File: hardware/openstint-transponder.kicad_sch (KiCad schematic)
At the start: 32 parts, among them J1 V+, J2 V-, Q1 AO3401A, U1 STM32C011F4Ux, U3 UCC27517DBV, U4 TLV760xx, Y1 20 MHz

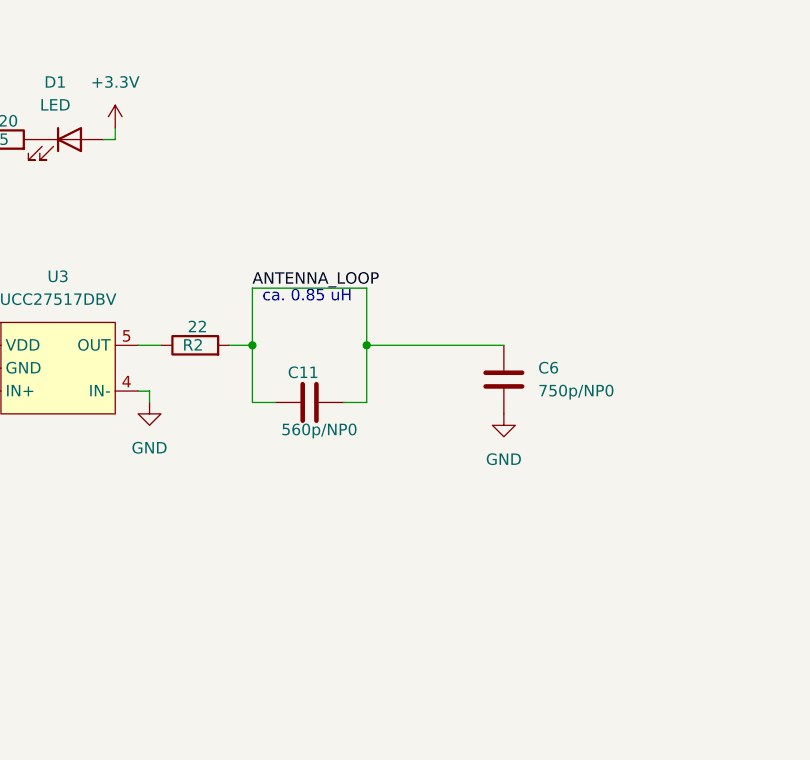
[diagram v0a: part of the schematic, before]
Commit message: antenna re-tuned
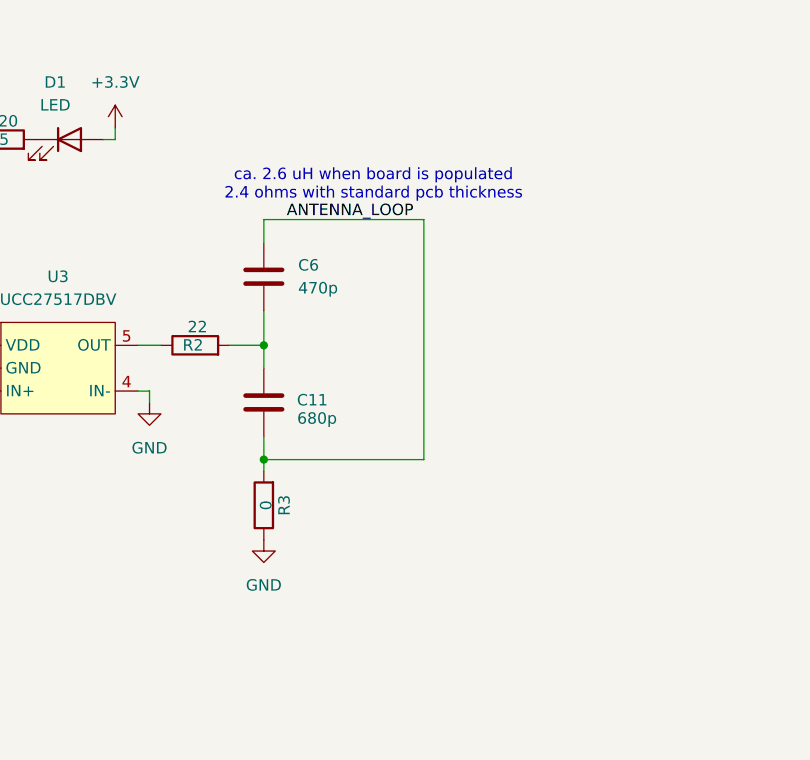
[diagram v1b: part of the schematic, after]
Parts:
- added R3: 0, Resistor_SMD:R_0402_1005Metric, symbol Device:R
- C11: value 560p/NP0 -> 680p; LCSC C107054 -> C30816
- C6: value 750p/NP0 -> 470p; LCSC C113798 -> C1620
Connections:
- net ANTENNA_LOOP: now also R3.2; no longer C11.1, R2.2
- net GND: now also R3.1; no longer C6.2
- new net: C11.1, C6.2, R2.2
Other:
- note added: "ca. 2.6 uH when board is populated 2.4 ohms with standard pcb thickness"
- note removed: "ca. 0.85 uH"
- moved on the sheet: C11, C6
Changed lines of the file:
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@@
 	(generator_version "9.0")
 	(paper "A4")
-	(text "ca. 0.85 uH"
+	(text "ca. 2.6 uH when board is populated\n2.4 ohms with standard pcb thickness"
 		(exclude_from_sim no)
-		(at 185.166 117.856 0)
+		(at 192.532 105.41 0)
 		(effects
 			(font
@@
 	)
 	(junction
-		(at 179.07 123.19)
+		(at 180.34 135.89)
 		(diameter 0)
 		(color 0 0 0 0)
@@
 	)
 	(junction
-		(at 191.77 123.19)
+		(at 180.34 123.19)
 		(diameter 0)
 		(color 0 0 0 0)
@@
 	(wire
 		(pts
+			(xy 180.34 111.76) (xy 180.34 109.22)
+		)
+		(stroke
+			(width 0)
+			(type default)
+		)
+	)
+	(wire
+		(pts
 			(xy 196.85 49.53) (xy 196.85 64.77)
 		)
@@
 	(wire
 		(pts
-			(xy 191.77 116.84) (xy 191.77 123.19)
+			(xy 198.12 109.22) (xy 198.12 135.89)
 		)
 		(stroke
@@
 	(wire
 		(pts
-			(xy 191.77 123.19) (xy 191.77 129.54)
-		)
-		(stroke
-			(width 0)
-			(type default)
-		)
-	)
-	(wire
-		(pts
 			(xy 116.84 118.11) (xy 116.84 119.38)
 		)
@@
 	(wire
 		(pts
-			(xy 127 119.38) (xy 129.54 119.38)
+			(xy 180.34 123.19) (xy 180.34 125.73)
 		)
 		(stroke
@@
 	(wire
 		(pts
-			(xy 33.02 49.53) (xy 33.02 50.8)
+			(xy 127 119.38) (xy 129.54 119.38)
 		)
 		(stroke
@@
 	(wire
 		(pts
-			(xy 207.01 123.19) (xy 191.77 123.19)
+			(xy 33.02 49.53) (xy 33.02 50.8)
 		)
 		(stroke
@@
 	(wire
 		(pts
+			(xy 180.34 133.35) (xy 180.34 135.89)
+		)
+		(stroke
+			(width 0)
+			(type default)
+		)
+	)
+	(wire
+		(pts
 			(xy 214.63 43.18) (xy 214.63 44.45)
 		)
@@
 	(wire
 		(pts
-			(xy 176.53 123.19) (xy 179.07 123.19)
+			(xy 176.53 123.19) (xy 180.34 123.19)
 		)
 		(stroke
@@
 	(wire
 		(pts
-			(xy 189.23 129.54) (xy 191.77 129.54)
+			(xy 68.58 43.18) (xy 74.93 43.18)
 		)
 		(stroke
@@
 	(wire
 		(pts
-			(xy 68.58 43.18) (xy 74.93 43.18)
+			(xy 180.34 119.38) (xy 180.34 123.19)
 		)
 		(stroke
@@
 	(wire
 		(pts
-			(xy 179.07 123.19) (xy 179.07 116.84)
-		)
-		(stroke
-			(width 0)
-			(type default)
-		)
-	)
-	(wire
-		(pts
 			(xy 167.64 129.54) (xy 167.64 128.27)
 		)
@@
 	(wire
 		(pts
-			(xy 179.07 129.54) (xy 179.07 123.19)
+			(xy 180.34 109.22) (xy 198.12 109.22)
 		)
 		(stroke
@@
 	(wire
 		(pts
+			(xy 180.34 135.89) (xy 180.34 137.16)
+		)
+		(stroke
+			(width 0)
+			(type default)
+		)
+	)
+	(wire
+		(pts
 			(xy 83.82 22.86) (xy 83.82 21.59)
 		)
@@
 	(wire
 		(pts
-			(xy 181.61 129.54) (xy 179.07 129.54)
+			(xy 274.32 59.69) (xy 274.32 58.42)
 		)
 		(stroke
@@
 	(wire
 		(pts
-			(xy 274.32 59.69) (xy 274.32 58.42)
+			(xy 158.75 44.45) (xy 171.45 44.45)
 		)
 		(stroke
@@
 	(wire
 		(pts
-			(xy 158.75 44.45) (xy 171.45 44.45)
+			(xy 54.61 49.53) (xy 55.88 49.53)
 		)
 		(stroke
@@
 	(wire
 		(pts
-			(xy 54.61 49.53) (xy 55.88 49.53)
+			(xy 180.34 135.89) (xy 198.12 135.89)
 		)
 		(stroke
@@
 		)
 	)
-	(wire
-		(pts
-			(xy 179.07 116.84) (xy 191.77 116.84)
-		)
-		(stroke
-			(width 0)
-			(type default)
-		)
-	)
 	(label "V_PUSHPULL"
 		(at 130.81 119.38 0)
@@
 	)
 	(label "ANTENNA_LOOP"
-		(at 179.07 116.84 0)
+		(at 182.88 109.22 0)
 		(effects
 			(font
@@
 	(symbol
 		(lib_id "Device:C")
-		(at 207.01 127 0)
+		(at 180.34 115.57 0)
 		(unit 1)
 		(exclude_from_sim no)
@@
 		(fields_autoplaced yes)
 		(property "Reference" "C6"
-			(at 210.82 125.7299 0)
+			(at 184.15 114.2999 0)
 			(effects
 				(font
@@
 			)
 		)
-		(property "Value" "750p/NP0"
-			(at 210.82 128.2699 0)
+		(property "Value" "470p"
+			(at 184.15 116.8399 0)
 			(effects
 				(font
@@
 		)
 		(property "Footprint" "Capacitor_SMD:C_0603_1608Metric"
-			(at 207.9752 130.81 0)
+			(at 181.3052 119.38 0)
 			(effects
 				(font
@@
 		)
 		(property "Datasheet" "~"
-			(at 207.01 127 0)
+			(at 180.34 115.57 0)
 			(effects
 				(font
@@
 		)
 		(property "Description" "Unpolarized capacitor"
-			(at 207.01 127 0)
+			(at 180.34 115.57 0)
 			(effects
 				(font
@@
 			)
 		)
-		(property "LCSC" "C113798"
-			(at 207.01 127 90)
+		(property "LCSC" "C1620"
+			(at 180.34 115.57 90)
 			(effects
 				(font
@@
 	(symbol
 		(lib_id "power:GND")
-		(at 207.01 130.81 0)
+		(at 180.34 144.78 0)
 		(unit 1)
 		(exclude_from_sim no)
@@
 		(fields_autoplaced yes)
 		(property "Reference" "#PWR019"
-			(at 207.01 137.16 0)
+			(at 180.34 151.13 0)
 			(effects
 				(font
@@
 		)
 		(property "Value" "GND"
-			(at 207.01 135.89 0)
+			(at 180.34 149.86 0)
 			(effects
 				(font
@@
 		)
 		(property "Footprint" ""
-			(at 207.01 130.81 0)
+			(at 180.34 144.78 0)
 			(effects
 				(font
@@
 		)
 		(property "Datasheet" ""
-			(at 207.01 130.81 0)
+			(at 180.34 144.78 0)
 			(effects
 				(font
@@
 		)
 		(property "Description" "Power symbol creates a global label with name \"GND\" , ground"
-			(at 207.01 130.81 0)
+			(at 180.34 144.78 0)
 			(effects
 				(font
@@
 	(symbol
 		(lib_id "Device:C")
-		(at 185.42 129.54 270)
+		(at 180.34 129.54 0)
 		(unit 1)
 		(exclude_from_sim no)
@@
 		(dnp no)
 		(property "Reference" "C11"
-			(at 186.436 126.238 90)
+			(at 187.452 129.286 0)
 			(effects
 				(font
@@
 			)
 		)
-		(property "Value" "560p/NP0"
-			(at 190.754 132.588 90)
+		(property "Value" "680p"
+			(at 188.468 131.318 0)
 			(effects
 				(font
@@
 		)
 		(property "Footprint" "Capacitor_SMD:C_0603_1608Metric"
-			(at 181.61 130.5052 0)
+			(at 181.3052 133.35 0)
 			(effects
 				(font
@@
 		)
 		(property "Datasheet" "~"
-			(at 185.42 129.54 0)
+			(at 180.34 129.54 0)
 			(effects
 				(font
@@
 		)
 		(property "Description" "Unpolarized capacitor"
-			(at 185.42 129.54 0)
+			(at 180.34 129.54 0)
 			(effects
 				(font
@@
 			)
 		)
-		(property "LCSC" "C107054"
-			(at 185.42 129.54 90)
+		(property "LCSC" "C30816"
+			(at 180.34 129.54 90)
 			(effects
 				(font
@@
 					(unit 1)
 				)
+			)
+		)
+	)
+	(symbol
+		(lib_id "Device:R")
+		(at 180.34 140.97 180)
+		(unit 1)
+		(exclude_from_sim no)
+		(in_bom yes)
+		(on_board yes)
+		(dnp no)
+		(property "Reference" "R3"
+			(at 182.626 140.97 90)
+			(effects
+				(font
+					(size 1.27 1.27)
+				)
+			)
+		)
+		(property "Value" "0"
+			(at 180.594 140.97 90)
+			(effects
+				(font
+					(size 1.27 1.27)
+				)
+			)
+		)
+		(property "Footprint" "Resistor_SMD:R_0402_1005Metric"
+			(at 182.118 140.97 90)
+			(effects
+				(font
+					(size 1.27 1.27)
+				)
+				(hide yes)
+			)
+		)
+		(property "Datasheet" "~"
+			(at 180.34 140.97 0)
+			(effects
+				(font
+					(size 1.27 1.27)
+				)
+				(hide yes)
+			)
+		)
+		(property "Description" "Resistor"
+			(at 180.34 140.97 0)
+			(effects
+				(font
+					(size 1.27 1.27)
+				)
+				(hide yes)
+			)
+		)
+		(pin "1"
+		)
+		(pin "2"
+		)
+		(instances
+			(project ""
+				(path "/df3d3e4d-85f7-40e4-bee7-39f1a9914bd0"
+					(reference "R3")
+					(unit 1)
+				)

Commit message: readme update
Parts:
- R3: LCSC (none) -> C17168
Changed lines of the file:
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@@
+			)
+		)
+		(property "LCSC" "C17168"
+			(at 180.34 140.97 90)
+			(effects
+				(font
+					(size 1.27 1.27)
+				)
+				(hide yes)
 			)
 		)

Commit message: v2 transponder
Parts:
- removed D2: 9.1V, Diode_SMD:D_SOD-323, symbol Device:D_Zener
- removed L1: 68n, Inductor_SMD:L_0603_1608Metric, symbol Device:L
- removed Q1: AO3401A, Package_TO_SOT_SMD:SOT-23, symbol Transistor_FET:AO3401A
- removed TP5: TestPoint, TestPoint:TestPoint_Pad_D1.0mm, symbol Connector:TestPoint
- removed U1: STM32C011F4Ux, Package_DFN_QFN:ST_UFQFPN-20_3x3mm_P0.5mm, symbol MCU_ST_STM32C0:STM32C011F4Ux
- removed U3: UCC27517DBV, Package_TO_SOT_SMD:SOT-23-5, symbol Driver_FET:UCC27517DBV
- removed U4: TLV760xx, Package_TO_SOT_SMD:SOT-23, symbol Regulator_Linear:TLV760xx
- removed Y1: 20 MHz, Crystal:Crystal_SMD_3225-4Pin_3.2x2.5mm, symbol Device:Crystal_GND24
- added AE1: Antenna_Loop, symbol Device:Antenna_Loop
- added C13, C14: 22p, Capacitor_SMD:C_0402_1005Metric, symbol Device:C
- added C15: 10u, Capacitor_SMD:C_0402_1005Metric, symbol Device:C
- added L2, L3: 3.3u, Inductor_SMD:L_0603_1608Metric, symbol Device:L
- added Q1: PMGD280UN, Package_TO_SOT_SMD:SOT-363_SC-70-6, symbol Transistor_FET:Q_Dual_NMOS_S1G1D2S2G2D1
- added R4: 22, Resistor_SMD:R_0402_1005Metric, symbol Device:R
- added R6, R7: 100k, Resistor_SMD:R_0402_1005Metric, symbol Device:R
- added U1: ATtiny1616-M, Package_DFN_QFN:VQFN-20-1EP_3x3mm_P0.4mm_EP1.7x1.7mm, symbol MCU_Microchip_ATtiny:ATtiny1616-M
- added U2: 10 MHz, Crystal:Crystal_SMD_3225-4Pin_3.2x2.5mm, symbol symbols:Oscillator
- added U3: SPX3819M5-L-3-3, Package_TO_SOT_SMD:SOT-23-5, symbol Regulator_Linear:SPX3819M5-L-3-3
- C1: value 4.7u/16V -> 10u; footprint Capacitor_SMD:C_0603_1608Metric -> Capacitor_SMD:C_0402_1005Metric; LCSC C19666 -> C15525
- C10: value 4.7u/16V -> 100n; footprint Capacitor_SMD:C_0603_1608Metric -> Capacitor_SMD:C_0402_1005Metric; LCSC C19666 -> C1525
- C11: value 680p -> 1n; footprint Capacitor_SMD:C_0603_1608Metric -> Capacitor_SMD:C_0402_1005Metric; LCSC C30816 -> C1523; now not fitted
- C4: value 20p -> 100n; LCSC C1554 -> C1525
- C5: value 20p -> 10n; LCSC C1554 -> C15195
- C6: value 470p -> 1n; footprint Capacitor_SMD:C_0603_1608Metric -> Capacitor_SMD:C_0402_1005Metric; LCSC C1620 -> C1523
- R1: value 220 -> 22; LCSC C25091 -> C25092
- R3: value 0 -> 22; LCSC C17168 -> C25092
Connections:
- net VFILT+ is gone; now on net GND: FL1.3
- net V_PUSHPULL is gone; now on net +3.3V: C1.1
- net +3.3V: now also C10.2, C2.2, C4.2, R3.2, C15.1, R4.2, U1.4 (VCC), U2.4 (VDD), U3.5 (OUT)
- net GND: now also C10.1, C2.1, C5.2, C13.1, C14.2, C15.2, Q1.1 (S), Q1.4 (S), R6.2, R7.2, U1.21 (GND), U1.3 (GND), U2.2 (GND), U3.2 (GND); no longer C10.2, C2.2, C5.1, FL1.4, R1.1, R3.1
- net VDDA: now also FL1.4, U3.1 (IN), U3.3 (EN); no longer C10.1
- net VIN+: now also FL1.1; no longer FL1.2
- net VIN-: now also FL1.2; no longer FL1.1
- net ~{BLINKY}: now also U1.6 (PA5)
- net GANT-: now reaches R2.1
- net GANT-: now also Q1.5 (G), R7.1
- removed net ANTENNA_LOOP: C11.2, C6.1, R3.2
- net SWDIO renamed UART0TXD
- net UART0TXD: now also U1.20 (PA1)
- net revpol_gate renamed GANT+
- net GANT+: now also Q1.2 (G), R6.1
- net ~{RST} renamed UDPI
- net UDPI: now also U1.19 (~{RESET}/PA0); no longer C2.1
- new net: C5.1, U3.4 (BP)
- new net: L2.1, R3.1
- new net: L3.1, R4.1
- new net A+: AE1.1, C11.1, C13.2, C6.1, L2.2, Q1.6 (D)
- new net A-: AE1.2, C11.2, C14.1, C6.2, L3.2, Q1.3 (D)
- new net ANT+: R1.1, U1.5 (PA4)
- new net ANT-: R2.2, U1.8 (PA7)
- new net EXTCLK: U1.2 (PA3), U2.3 (OUT)
- no-connect marks 11 -> 13
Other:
- note added: "ANT signal is created by XOR & XNOR an internal CLK/2 signal with UART-TxD, TP2 helps debugging"
- note added: "INPUT FILTER"
- note added: "LDO /W REVERSE POL. PROT."
- note added: "TODO: try wirewounds as well"
- note added: "alternatives: MAX1725, MAX1726 MIC5205, MIC5225, MIC5233 SPX3819, SPX5205"
- note removed: "INPUT FILTER & REVERSE POLATITY PROTECTION"
- note removed: "ca. 2.6 uH when board is populated 2.4 ohms with standard pcb thickness"
- moved on the sheet: C7, C8, C9, D1, FL1, J1, J2, R5, TP1
